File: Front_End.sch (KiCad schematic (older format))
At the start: 0 parts

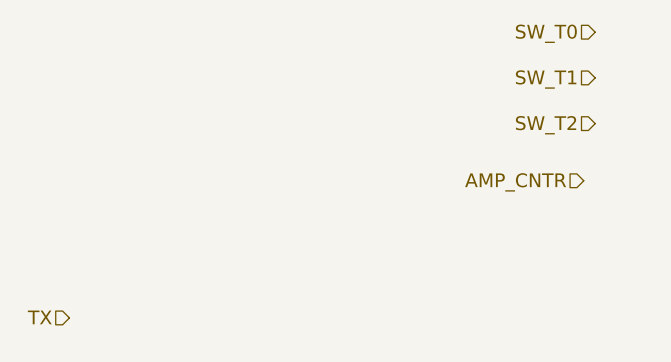
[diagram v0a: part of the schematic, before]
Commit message: deleted MCU schematic for v0.1. Added power sub-schematic
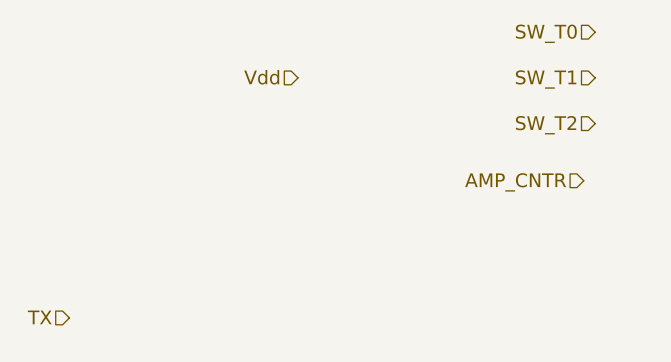
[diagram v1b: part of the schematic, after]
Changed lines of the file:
@@
 Text HLabel 1700 2800 0    60   Input ~ 0
 RX
+Text HLabel 2700 1450 0    60   Input ~ 0
+Vdd
 $EndSCHEMATC

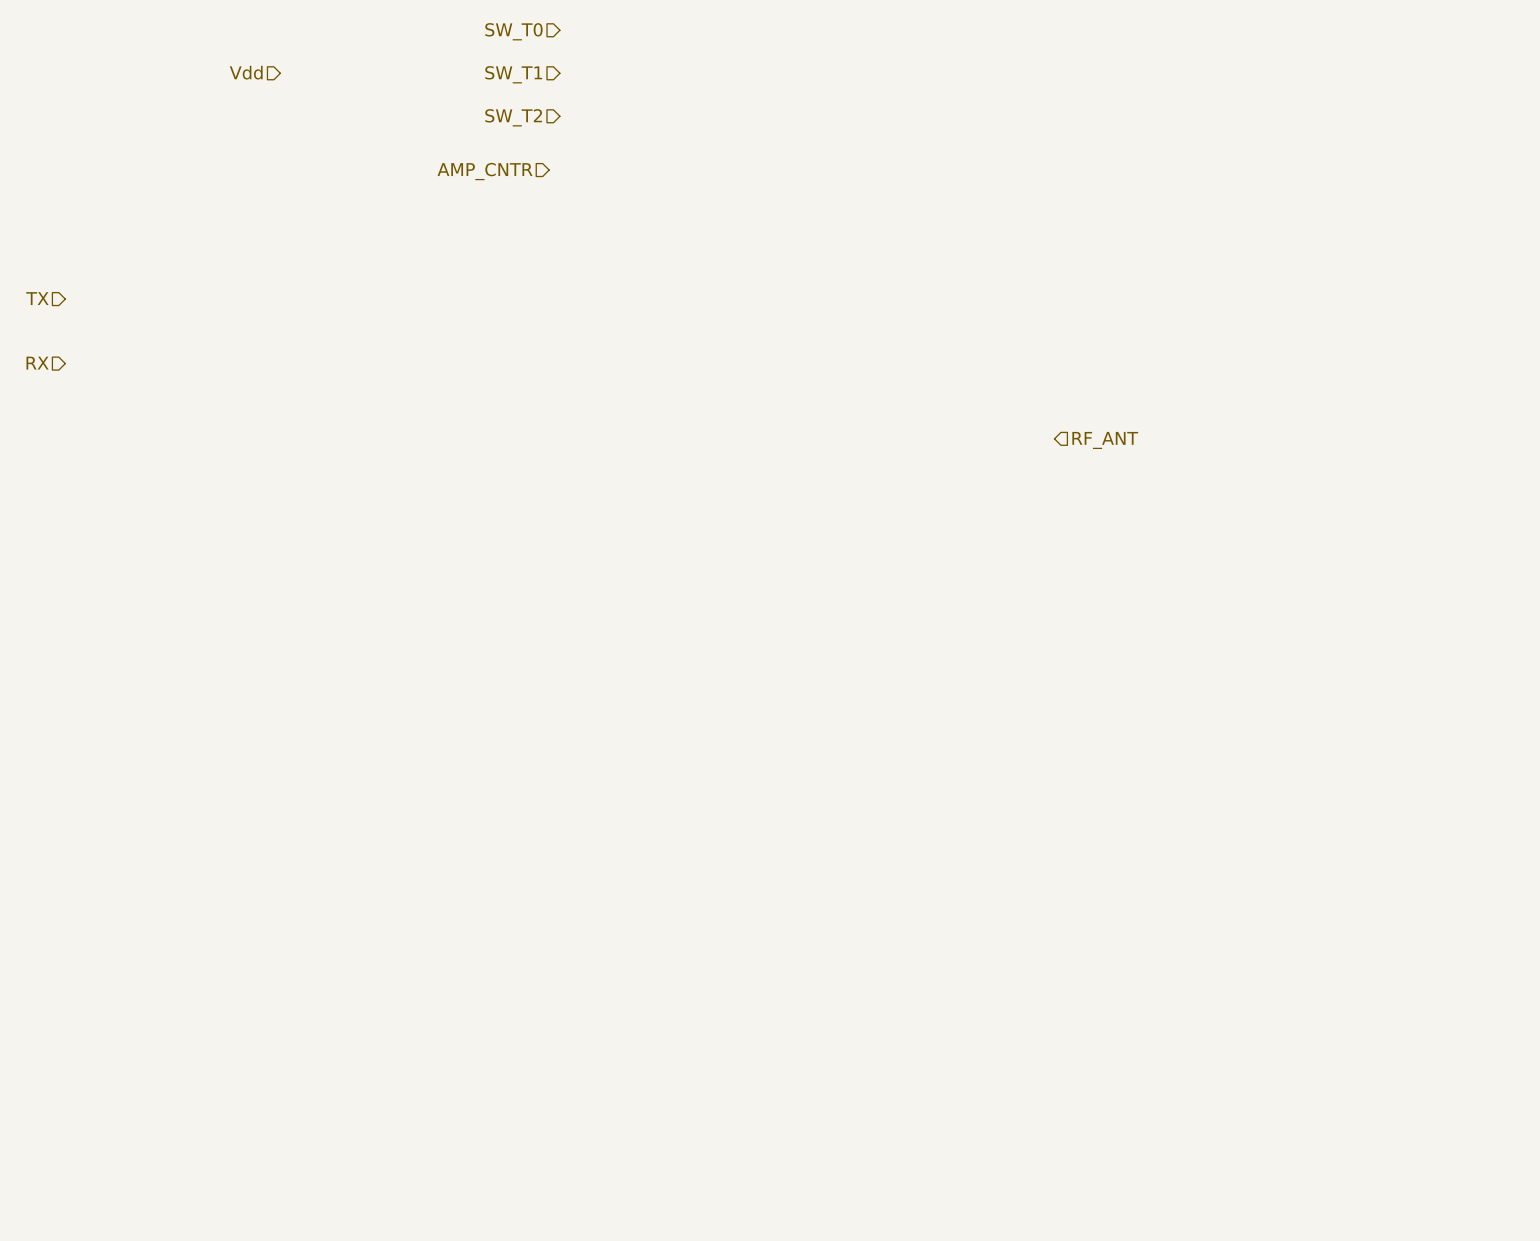
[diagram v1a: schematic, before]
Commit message: added SKY65366-21 schematic and footprint to library. Populated front end schematic with SKY and peripherial components. Added 3V6 output for power sub-schematic.
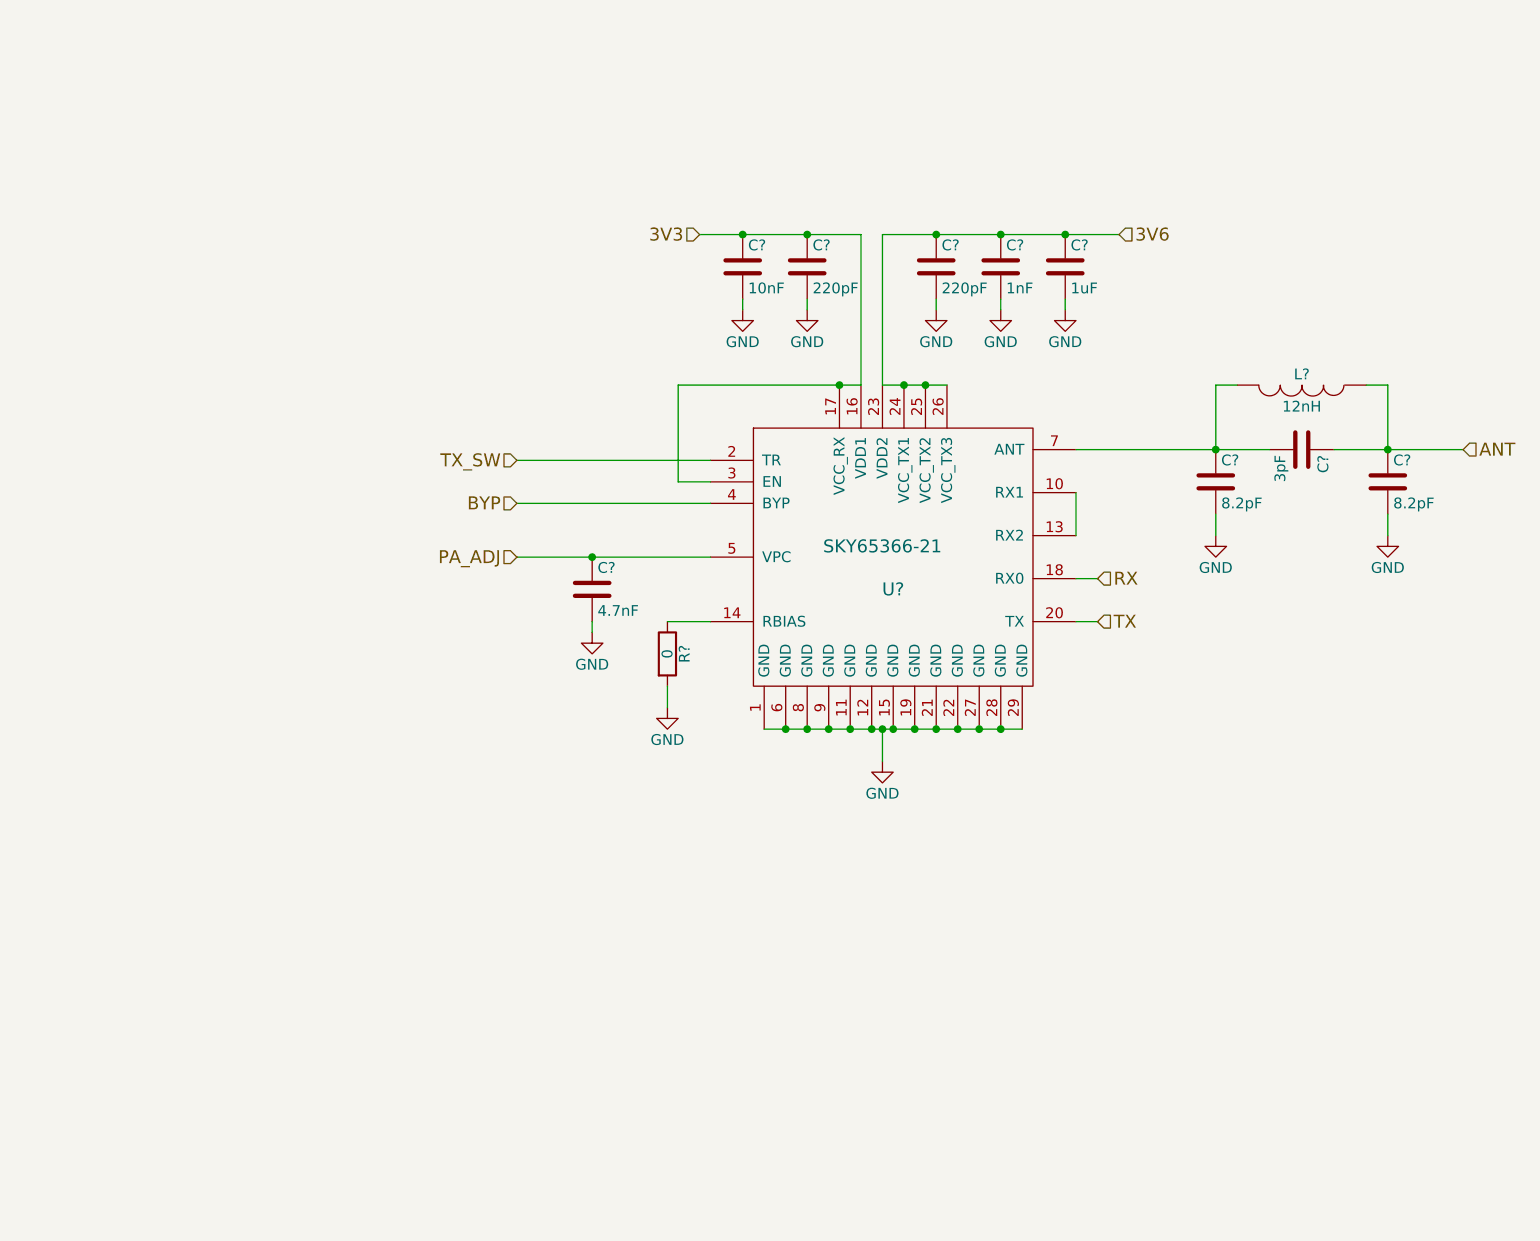
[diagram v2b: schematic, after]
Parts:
- added C? (x2): 220pF, symbol C
- added C?: 1nF, symbol C
- added C?: 1uF, symbol C
- added C?: 10nF, symbol C
- added C?: 3pF, symbol C
- added C? (x2): 8.2pF, symbol C
- added C?: 4.7nF, symbol C
- added L?: 12nH, symbol INDUCTOR
- added R?: 0, symbol R
- added U?: SKY65366-21, symbol SKY65366-21
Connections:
- net RX: now also U?.18 (RX0)
- net TX: now also U?.20 (TX)
- new net: U?.10 (RX1), U?.13 (RX2)
- new net: R?.1, U?.14 (RBIAS)
- new net: C?.1, C?.2, L?.2, U?.7 (ANT)
- new net 3V3: C?.1, C?.1, U?.16 (VDD1), U?.17 (VCC_RX), U?.3 (EN)
- new net 3V6: C?.1, C?.1, C?.1, U?.23 (VDD2), U?.24 (VCC_TX1), U?.25 (VCC_TX2), U?.26 (VCC_TX3)
- new net ANT: C?.1, C?.1, L?.1
- new net BYP: U?.4 (BYP)
- new net GND: C?.2, C?.2, C?.2, C?.2, C?.2, C?.2, C?.2, C?.2, R?.2, U?.1 (GND), U?.11 (GND), U?.12 (GND), U?.15 (GND), U?.19 (GND), U?.21 (GND), U?.22 (GND), U?.27 (GND), U?.28 (GND), U?.29 (GND), U?.6 (GND), U?.8 (GND), U?.9 (GND)
- new net PA_ADJ: C?.1, U?.5 (VPC)
- new net TX_SW: U?.2 (TR)

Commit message: cleanup
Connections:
- net 3V3: no longer U?.3 (EN)
- new net EN: U?.3 (EN)
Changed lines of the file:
@@
 $EndComp
 $Comp
-L GND #PWR?
+L GND #PWR021
 U 1 1 58719F72
 P 5500 4650
-F 0 "#PWR?" H 5500 4400 50  0001 C CNN
+F 0 "#PWR021" H 5500 4400 50  0001 C CNN
 F 1 "GND" H 5500 4500 50  0000 C CNN
 F 2 "" H 5500 4650 50  0000 C CNN
@@
 $EndComp
 $Comp
-L GND #PWR?
+L GND #PWR022
 U 1 1 5871BAFA
 P 5750 2550
-F 0 "#PWR?" H 5750 2300 50  0001 C CNN
+F 0 "#PWR022" H 5750 2300 50  0001 C CNN
 F 1 "GND" H 5750 2400 50  0000 C CNN
 F 2 "" H 5750 2550 50  0000 C CNN
@@
 $EndComp
 $Comp
-L GND #PWR?
+L GND #PWR023
 U 1 1 5871BB16
 P 6050 2550
-F 0 "#PWR?" H 6050 2300 50  0001 C CNN
+F 0 "#PWR023" H 6050 2300 50  0001 C CNN
 F 1 "GND" H 6050 2400 50  0000 C CNN
 F 2 "" H 6050 2550 50  0000 C CNN
@@
 $EndComp
 $Comp
-L GND #PWR?
+L GND #PWR024
 U 1 1 5871BB32
 P 6350 2550
-F 0 "#PWR?" H 6350 2300 50  0001 C CNN
+F 0 "#PWR024" H 6350 2300 50  0001 C CNN
 F 1 "GND" H 6350 2400 50  0000 C CNN
 F 2 "" H 6350 2550 50  0000 C CNN
@@
 $EndComp
 $Comp
-L GND #PWR?
+L GND #PWR025
 U 1 1 5871BD81
 P 5150 2550
-F 0 "#PWR?" H 5150 2300 50  0001 C CNN
+F 0 "#PWR025" H 5150 2300 50  0001 C CNN
 F 1 "GND" H 5150 2400 50  0000 C CNN
 F 2 "" H 5150 2550 50  0000 C CNN
@@
 $EndComp
 $Comp
-L GND #PWR?
+L GND #PWR026
 U 1 1 5871BDA1
 P 4850 2550
-F 0 "#PWR?" H 4850 2300 50  0001 C CNN
+F 0 "#PWR026" H 4850 2300 50  0001 C CNN
 F 1 "GND" H 4850 2400 50  0000 C CNN
 F 2 "" H 4850 2550 50  0000 C CNN
@@
 	4650 2200 5400 2200
 Wire Wire Line
-	4550 2900 5400 2900
+	5300 2900 5400 2900
 Connection ~ 4850 2200
 Wire Wire Line
@@
 	7050 2900 7050 3200
 $Comp
-L GND #PWR?
+L GND #PWR027
 U 1 1 5871C376
 P 7050 3600
-F 0 "#PWR?" H 7050 3350 50  0001 C CNN
+F 0 "#PWR027" H 7050 3350 50  0001 C CNN
 F 1 "GND" H 7050 3450 50  0000 C CNN
 F 2 "" H 7050 3600 50  0000 C CNN
@@
 $EndComp
 $Comp
-L GND #PWR?
+L GND #PWR028
 U 1 1 5871C39E
 P 7850 3600
-F 0 "#PWR?" H 7850 3350 50  0001 C CNN
+F 0 "#PWR028" H 7850 3350 50  0001 C CNN
 F 1 "GND" H 7850 3450 50  0000 C CNN
 F 2 "" H 7850 3600 50  0000 C CNN
@@
 $EndComp
 $Comp
-L GND #PWR?
+L GND #PWR029
 U 1 1 5871CA19
 P 4500 4400
-F 0 "#PWR?" H 4500 4150 50  0001 C CNN
+F 0 "#PWR029" H 4500 4150 50  0001 C CNN
 F 1 "GND" H 4500 4250 50  0000 C CNN
 F 2 "" H 4500 4400 50  0000 C CNN
@@
 $EndComp
 $Comp
-L GND #PWR?
+L GND #PWR030
 U 1 1 5871CD23
 P 4150 4050
-F 0 "#PWR?" H 4150 3800 50  0001 C CNN
+F 0 "#PWR030" H 4150 3800 50  0001 C CNN
 F 1 "GND" H 4150 3900 50  0000 C CNN
 F 2 "" H 4150 4050 50  0000 C CNN
@@
 	5500 2900 5500 2200
 Connection ~ 5750 2200
-Wire Wire Line
-	4700 3350 4550 3350
-Wire Wire Line
-	4550 3350 4550 2900
-Connection ~ 5300 2900
 Text HLabel 3800 3450 0    60   Input ~ 0
 BYP
@@
 Wire Wire Line
 	3800 3450 4700 3450
+Wire Wire Line
+	4700 3350 3800 3350
+Text HLabel 3800 3350 0    60   Input ~ 0
+EN
 $EndSCHEMATC

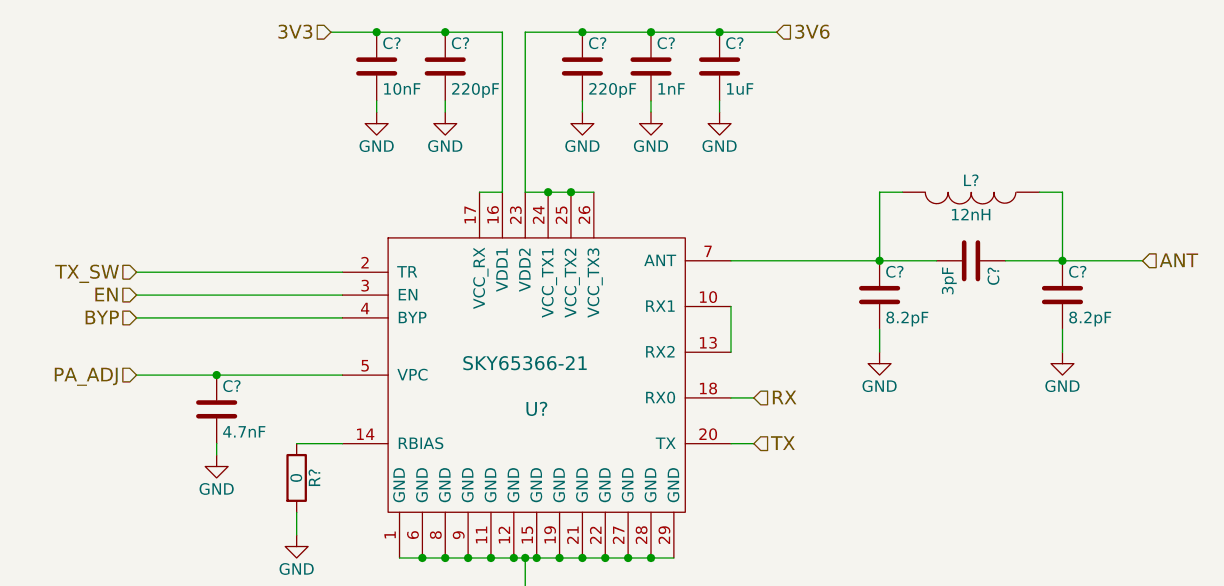
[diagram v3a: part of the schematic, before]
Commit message: Added RF switch to transciever schematic
-Removed SMA lib pointing to Tobi's downloads
-Added SKY13372-467LF to the library (symbol and decal)
-Renamed signal “TX_SW” on RF front end page to “TRX_SIG”
-Re-aligned some part names and reference designators
-Added some component values to the front end
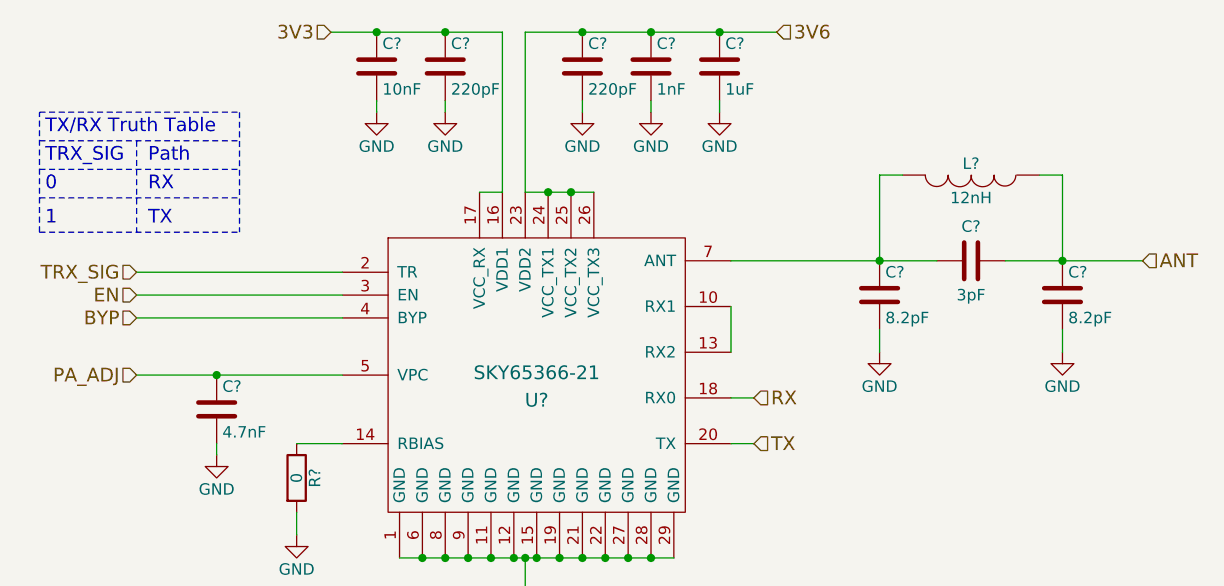
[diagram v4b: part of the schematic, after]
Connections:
- net TX_SW renamed TRX_SIG
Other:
- note added: "0"
- note added: "1\n"
- note added: "Path"
- note added: "RX"
- note added: "TRX_SIG"
- note added: "TX"
- note added: "TX/RX Truth Table"
- moved on the sheet: L?
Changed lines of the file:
@@
 U 1 1 58719E85
 P 5550 3750
-F 0 "U?" H 5550 3650 60  0000 C CNN
-F 1 "SKY65366-21" H 5500 3850 60  0000 C CNN
+F 0 "U?" H 5550 3725 60  0000 C TNN
+F 1 "SKY65366-21" H 5550 3775 60  0000 C BNN
 F 2 "" H 5550 3650 60  0000 C CNN
 F 3 "" H 5550 3650 60  0000 C CNN
@@
 U 1 1 5871C0B1
 P 7450 3200
-F 0 "C?" H 7475 3300 50  0000 L CNN
-F 1 "3pF" H 7475 3100 50  0000 L CNN
+F 0 "C?" V 7300 3200 50  0000 C CNN
+F 1 "3pF" V 7600 3200 50  0000 C CNN
 F 2 "" H 7488 3050 50  0000 C CNN
 F 3 "" H 7450 3200 50  0000 C CNN
@@
 L INDUCTOR L?
 U 1 1 5871C1AA
-P 7450 2900
-F 0 "L?" V 7400 2900 50  0000 C CNN
-F 1 "12nH" V 7550 2900 50  0000 C CNN
-F 2 "" H 7450 2900 50  0000 C CNN
-F 3 "" H 7450 2900 50  0000 C CNN
-	1    7450 2900
+P 7450 2825
+F 0 "L?" V 7400 2825 50  0000 C CNN
+F 1 "12nH" V 7550 2825 50  0000 C CNN
+F 2 "" H 7450 2825 50  0000 C CNN
+F 3 "" H 7450 2825 50  0000 C CNN
+	1    7450 2825
 	0    1    1    0
 $EndComp
@@
 Connection ~ 7850 3200
 Wire Wire Line
-	7750 2900 7850 2900
-Wire Wire Line
-	7850 2900 7850 3200
-Wire Wire Line
-	7150 2900 7050 2900
-Wire Wire Line
-	7050 2900 7050 3200
+	7850 2825 7850 3200
+Wire Wire Line
+	7150 2825 7050 2825
+Wire Wire Line
+	7050 2825 7050 3200
 $Comp
 L GND #PWR027
@@
 BYP
 Text HLabel 3800 3250 0    60   Input ~ 0
-TX_SW
+TRX_SIG
 Wire Wire Line
 	4700 3250 3800 3250
@@
 Text HLabel 3800 3350 0    60   Input ~ 0
 EN
+Text Notes 3400 2775 0    60   ~ 0
+TRX_SIG
+Text Notes 3400 2650 0    60   ~ 0
+TX/RX Truth Table
+Text Notes 3850 2775 0    60   ~ 0
+Path
+Text Notes 3400 2900 0    60   ~ 0
+0
+Text Notes 3400 3050 0    60   ~ 0
+1\n
+Text Notes 3850 2900 0    60   ~ 0
+RX
+Text Notes 3850 3050 0    60   ~ 0
+TX
+Wire Notes Line
+	3375 2925 4250 2925
+Wire Notes Line
+	3375 2800 4250 2800
+Wire Notes Line
+	3375 3075 4250 3075
+Wire Notes Line
+	3375 2675 4250 2675
+Wire Notes Line
+	3375 2550 4250 2550
+Wire Notes Line
+	4250 2550 4250 3075
+Wire Notes Line
+	3375 3075 3375 2550
+Wire Notes Line
+	3800 2675 3800 3075
+Wire Wire Line
+	7750 2825 7850 2825
 $EndSCHEMATC

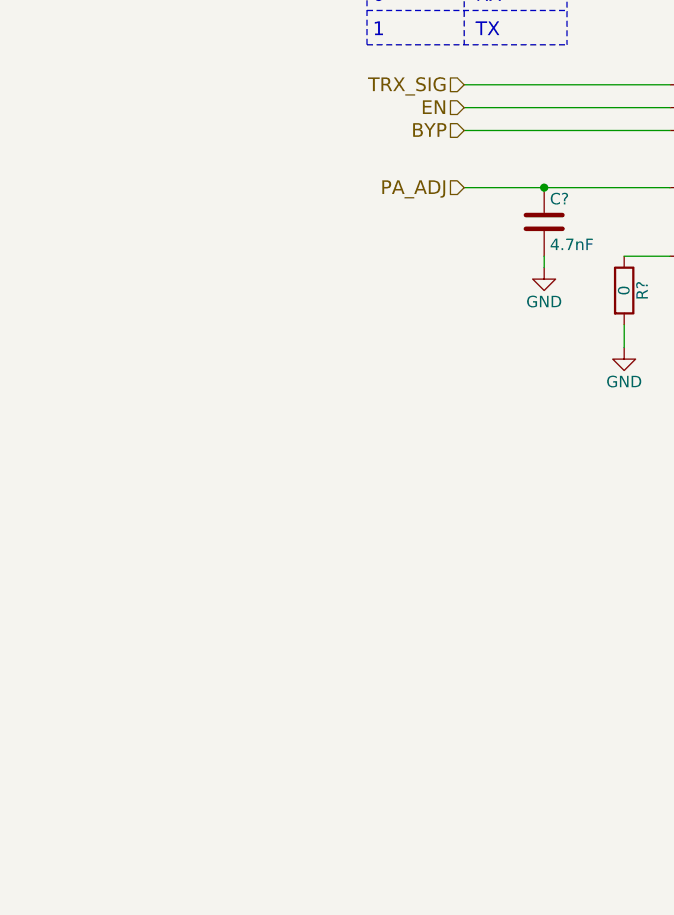
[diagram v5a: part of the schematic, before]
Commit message: moved jumpers into respective schematics
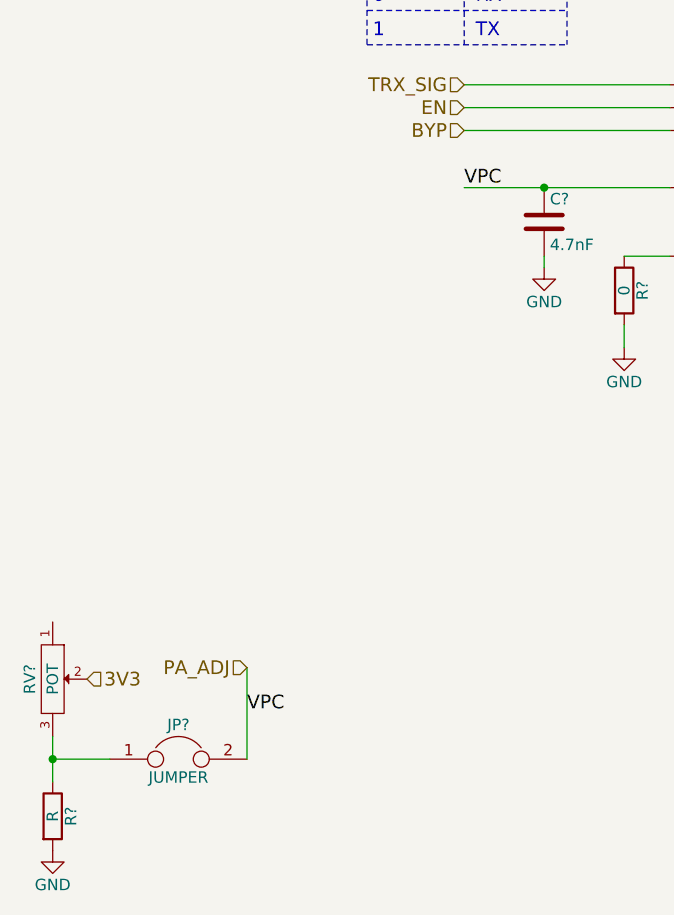
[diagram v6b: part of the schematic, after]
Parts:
- added JP?: JUMPER, symbol JUMPER
- added R?: R, symbol R
- added RV?: POT, symbol POT
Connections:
- net 3V3: now also RV?.2
- net GND: now also R?.2
- net PA_ADJ: now also JP?.2
- new net: JP?.1, R?.1, RV?.3
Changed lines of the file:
@@
 Text HLabel 8200 3200 2    60   Input ~ 0
 ANT
-Text HLabel 3800 3700 0    60   Input ~ 0
+Text HLabel 2850 5800 0    60   Input ~ 0
 PA_ADJ
 Text HLabel 6500 4000 2    60   Input ~ 0
@@
 Wire Wire Line
 	7750 2825 7850 2825
+$Comp
+L JUMPER JP?
+U 1 1 587C256C
+P 2550 6200
+F 0 "JP?" H 2550 6350 50  0000 C CNN
+F 1 "JUMPER" H 2550 6120 50  0000 C CNN
+F 2 "" H 2550 6200 50  0000 C CNN
+F 3 "" H 2550 6200 50  0000 C CNN
+	1    2550 6200
+	1    0    0    -1
+$EndComp
+$Comp
+L R R?
+U 1 1 587C3C10
+P 2000 6450
+F 0 "R?" V 2080 6450 50  0000 C CNN
+F 1 "R" V 2000 6450 50  0000 C CNN
+F 2 "" V 1930 6450 50  0000 C CNN
+F 3 "" H 2000 6450 50  0000 C CNN
+	1    2000 6450
+	1    0    0    -1
+$EndComp
+$Comp
+L GND #PWR?
+U 1 1 587C3C45
+P 2000 6600
+F 0 "#PWR?" H 2000 6350 50  0001 C CNN
+F 1 "GND" H 2000 6450 50  0000 C CNN
+F 2 "" H 2000 6600 50  0000 C CNN
+F 3 "" H 2000 6600 50  0000 C CNN
+	1    2000 6600
+	1    0    0    -1
+$EndComp
+Wire Wire Line
+	2000 6100 2000 6300
+Wire Wire Line
+	2250 6200 2000 6200
+Connection ~ 2000 6200
+Wire Wire Line
+	2850 6200 2850 5800
+Text Label 3800 3700 0    60   ~ 0
+VPC
+Text Label 2850 6000 0    60   ~ 0
+VPC
+Text HLabel 2150 5850 2    60   Input ~ 0
+3V3
+$Comp
+L POT RV?
+U 1 1 587CA745
+P 2000 5850
+F 0 "RV?" H 2000 5750 50  0000 C CNN
+F 1 "POT" H 2000 5850 50  0000 C CNN
+F 2 "" H 2000 5850 50  0000 C CNN
+F 3 "" H 2000 5850 50  0000 C CNN
+	1    2000 5850
+	0    1    1    0
+$EndComp
 $EndSCHEMATC
